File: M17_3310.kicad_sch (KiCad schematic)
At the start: 0 parts

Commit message: imported SA868 - thanks, edgetriggered
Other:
- sheet Interfaces ports: added 5V_USB, BOOT0, CLK, CMD, DAT0, DAT1, DAT2, DAT3, KEY_COLS, KEY_ROWS, PWM_BLIGHT, SD_DET, UDB_DM, USB_DP; removed none
- sheet MCU ports: added BOOT0, RF_RX, RF_TX, RTC_BATT, UDB_DM, USB_DP; removed none
- sheet PMU ports: added 5V_USB, PWR_ON, RTC_BATT, U_BATT, ~{CHG}; removed none
- sheet RF ports: added DEMOD_OUT, ENA, MOD_IN, PTT, PWR_SEL, RX, TX, U_BATT; removed none

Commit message: interfaces update
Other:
- sheet Interfaces ports: added DISP_D/C, DISP_SCK, DISP_SDIN, ~{DISP_CE}, ~{DISP_RST}; removed none
- sheet MCU ports: added DISP_DATA, DISP_D/C, DISP_SCK, KEY_COLS, KEY_ROWS, PTT_OUT, PWM_BLIGHT, RF_ENA, RF_PWR, ~{DISP_CE}, ~{DISP_RST}; removed none

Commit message: connections
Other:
- sheet MCU ports: added BSB_IN, BSB_OUT, PWR_ON, SD_CLK, SD_CMD, SD_D0, SD_D1, SD_D2, SD_D3, SD_DET, ~{CHG}; removed none

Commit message: audio part
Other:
- added sheet Audio (audio.kicad_sch)
- added sheet FIlters (filters.kicad_sch)
- sheet Interfaces ports: added VIBR; removed none
- sheet MCU ports: added AF_AMP_EN, MIC_IN, SPK_OUT, VIBR, ~{RF_ENA}; removed RF_ENA
- sheet RF ports: added ~{ENA}; removed ENA

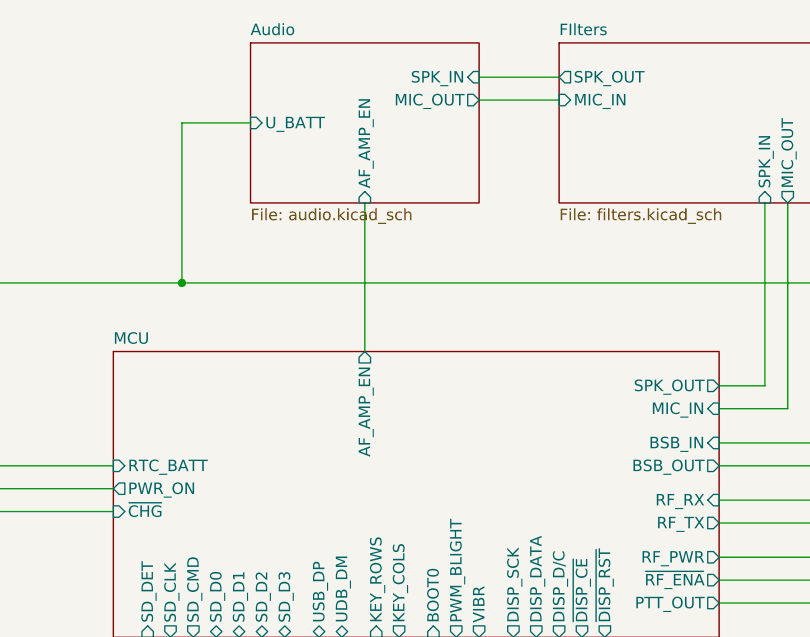
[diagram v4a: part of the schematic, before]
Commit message: spk/mic update
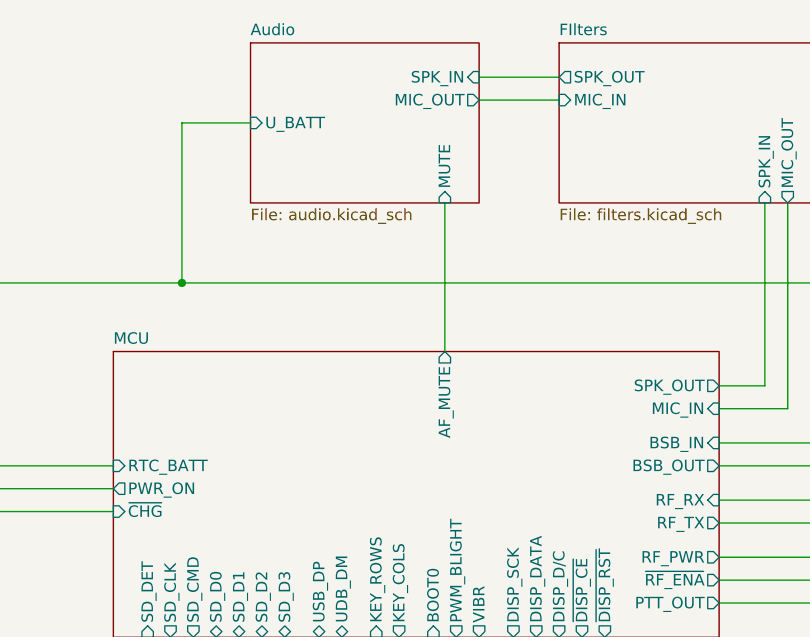
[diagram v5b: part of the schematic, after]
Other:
- sheet Audio ports: added MUTE; removed AF_AMP_EN
- sheet MCU ports: added AF_MUTE; removed AF_AMP_EN
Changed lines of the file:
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@@
 	(title_block
 		(title "Mainboard replacement for Nokia 3310")
-		(date "25-10-2024")
+		(date "28-10-2024")
 		(rev "Rev A")
 		(company "M17 Project")
@@
 	(wire
 		(pts
-			(xy 125.73 69.85) (xy 125.73 86.36)
+			(xy 134.62 69.85) (xy 134.62 86.36)
 		)
 		(stroke
@@
 			)
 		)
-		(pin "AF_AMP_EN" input
-			(at 125.73 69.85 270)
+		(pin "MUTE" input
+			(at 134.62 69.85 270)
 			(effects
 				(font
@@
 			)
 		)
-		(pin "AF_AMP_EN" output
-			(at 125.73 86.36 90)
-			(effects
-				(font
+		(pin "AF_MUTE" output
+			(at 134.62 86.36 90)
+			(effects
+				(font

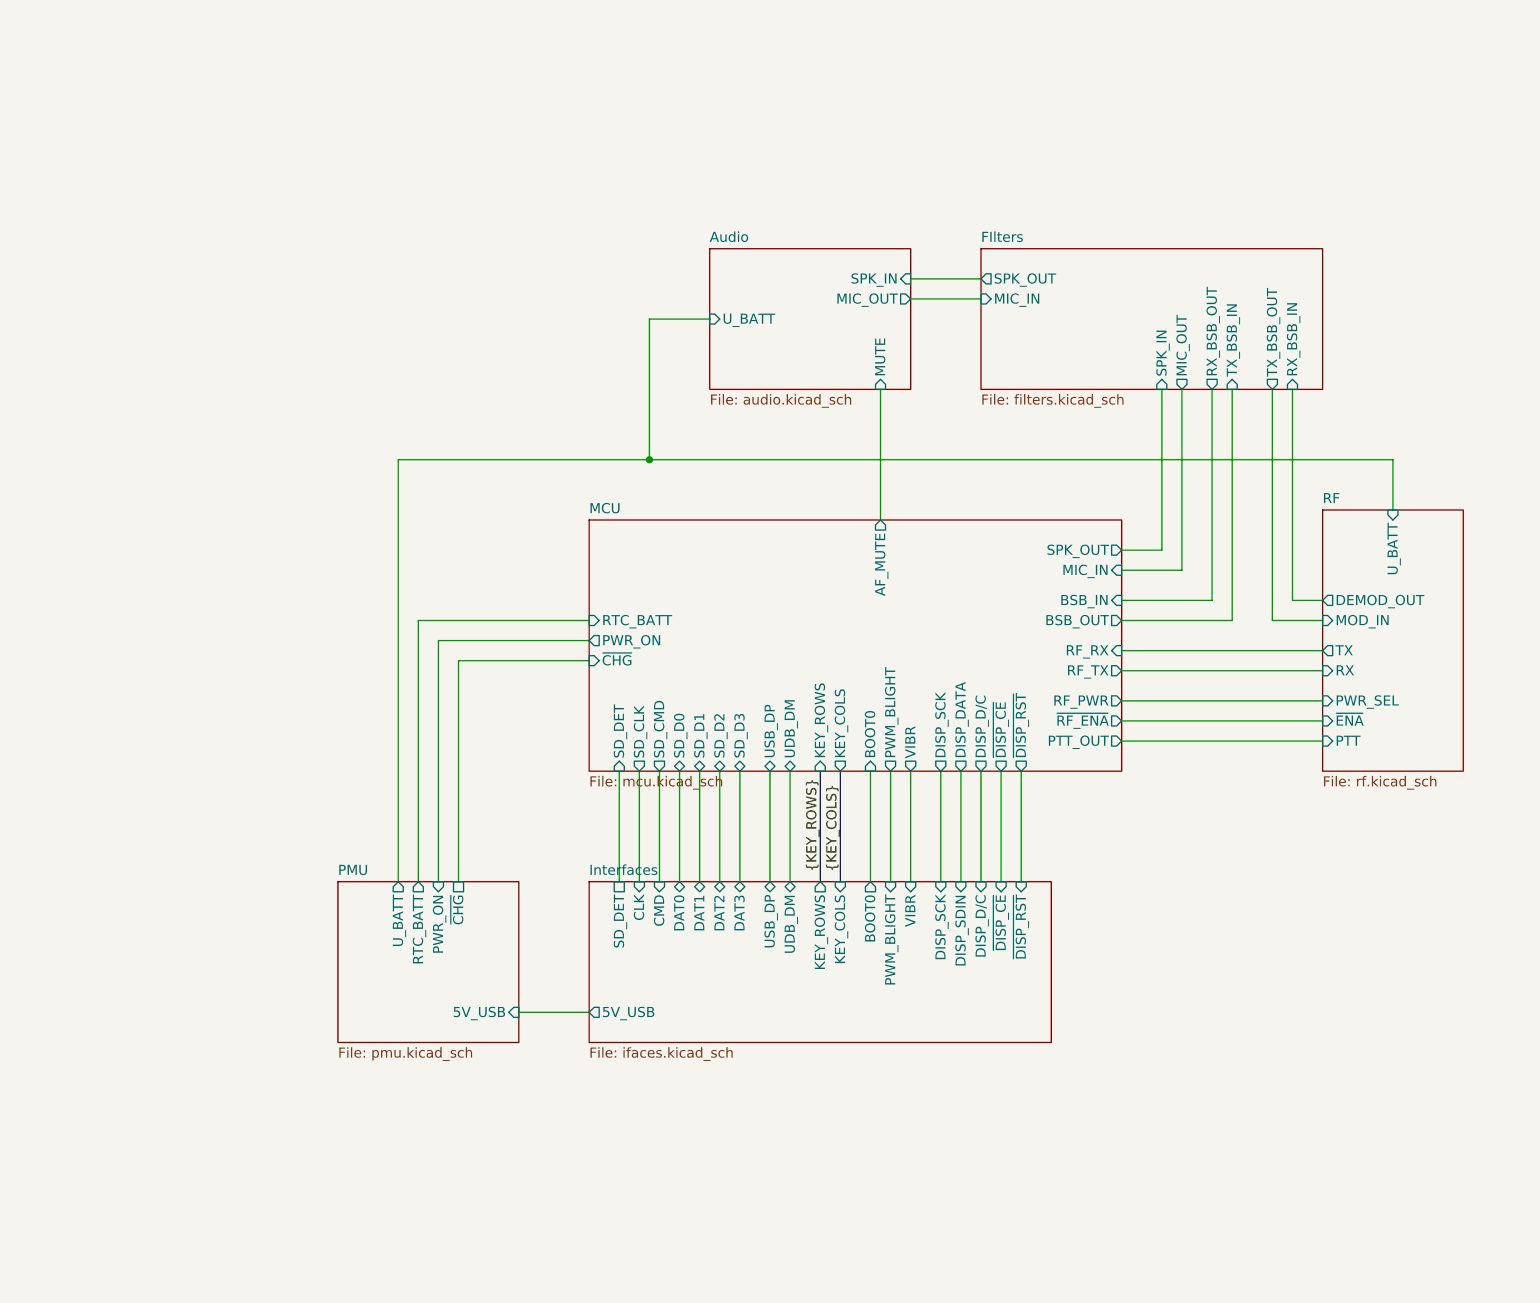
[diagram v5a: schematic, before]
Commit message: removed audio part
- added buzzer
- added battery voltage measurement
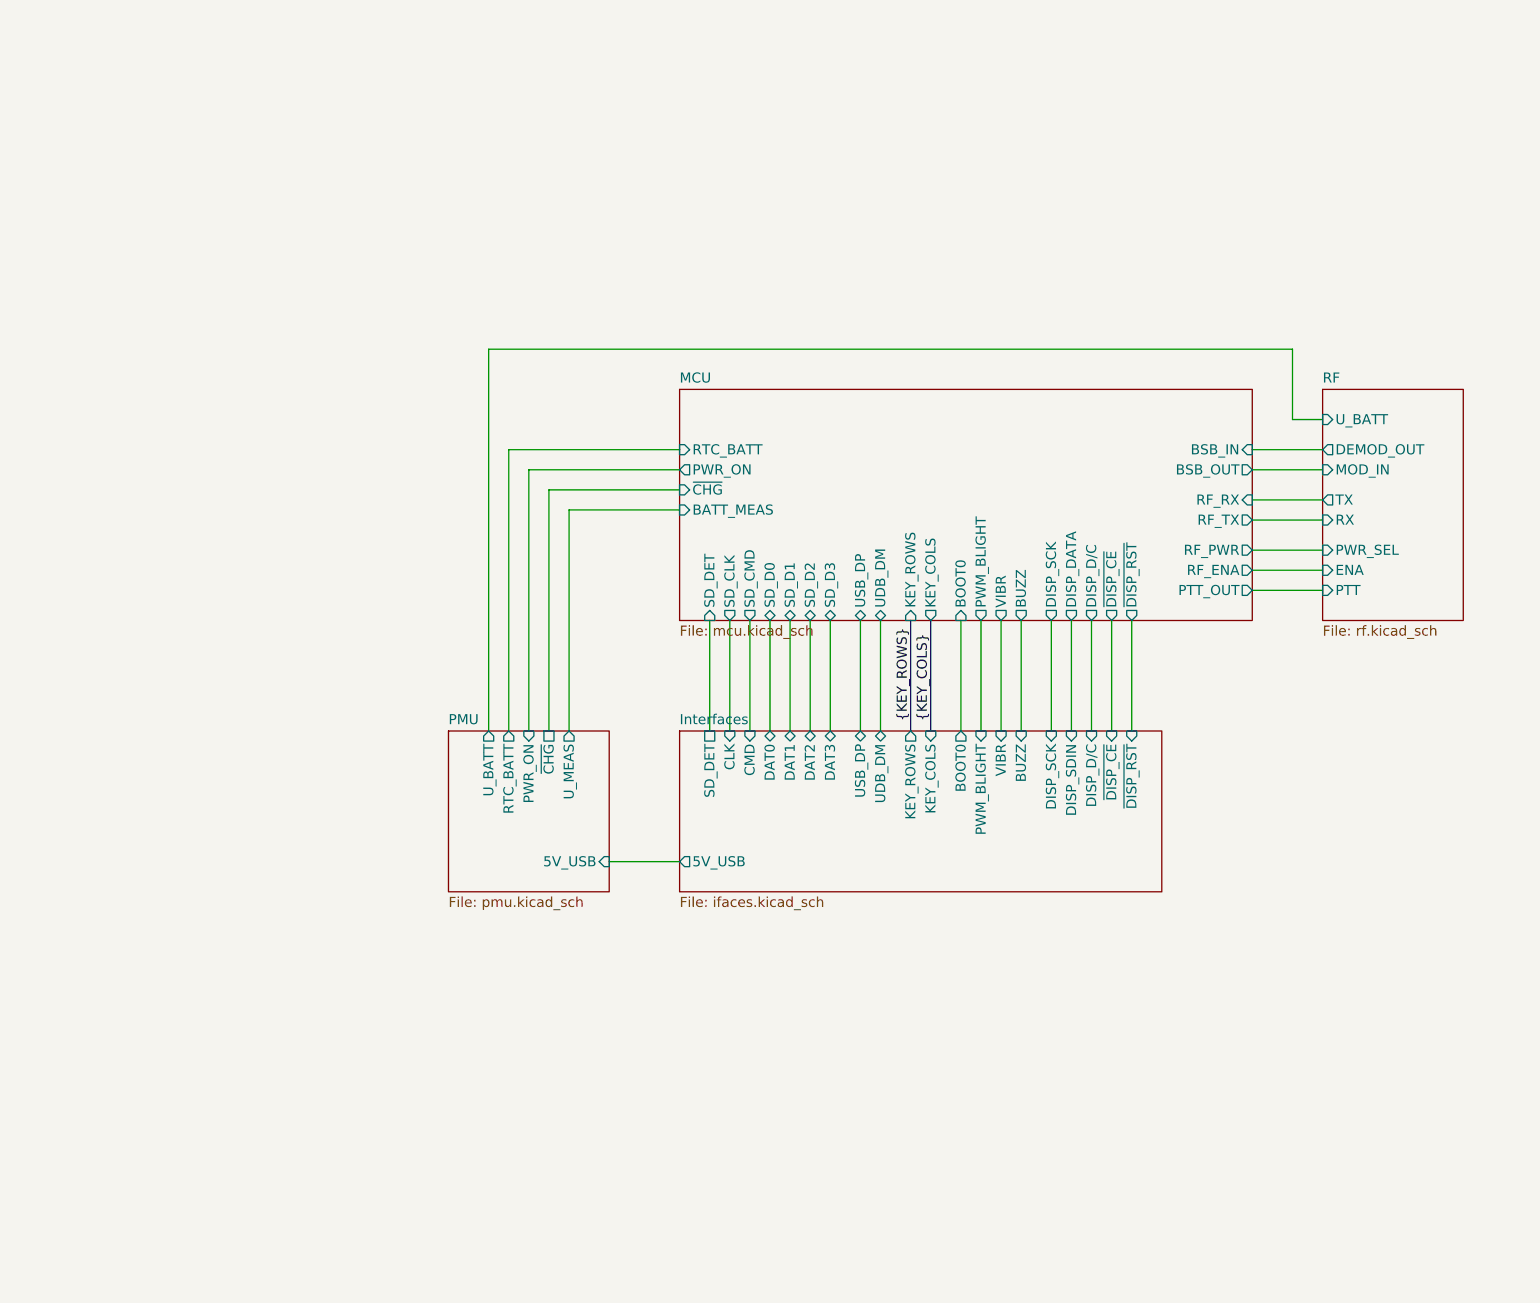
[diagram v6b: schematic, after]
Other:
- removed sheet Audio
- removed sheet FIlters
- sheet Interfaces ports: added BUZZ; removed none
- sheet MCU ports: added BATT_MEAS, BUZZ, RF_ENA; removed AF_MUTE, MIC_IN, SPK_OUT, ~{RF_ENA}
- sheet PMU ports: added U_MEAS; removed none
- sheet RF ports: added ENA; removed ~{ENA}

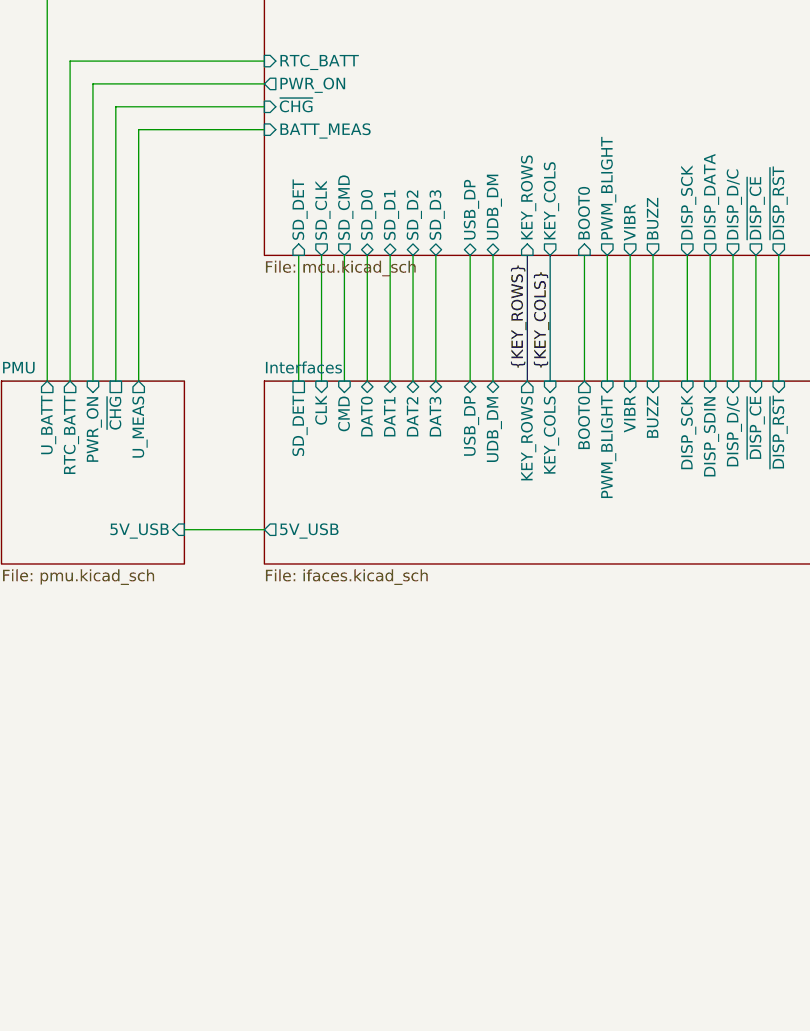
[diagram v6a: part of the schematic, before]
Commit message: mayhem
- removed sd card slot
- started pcb design
- added nice 3310 photos
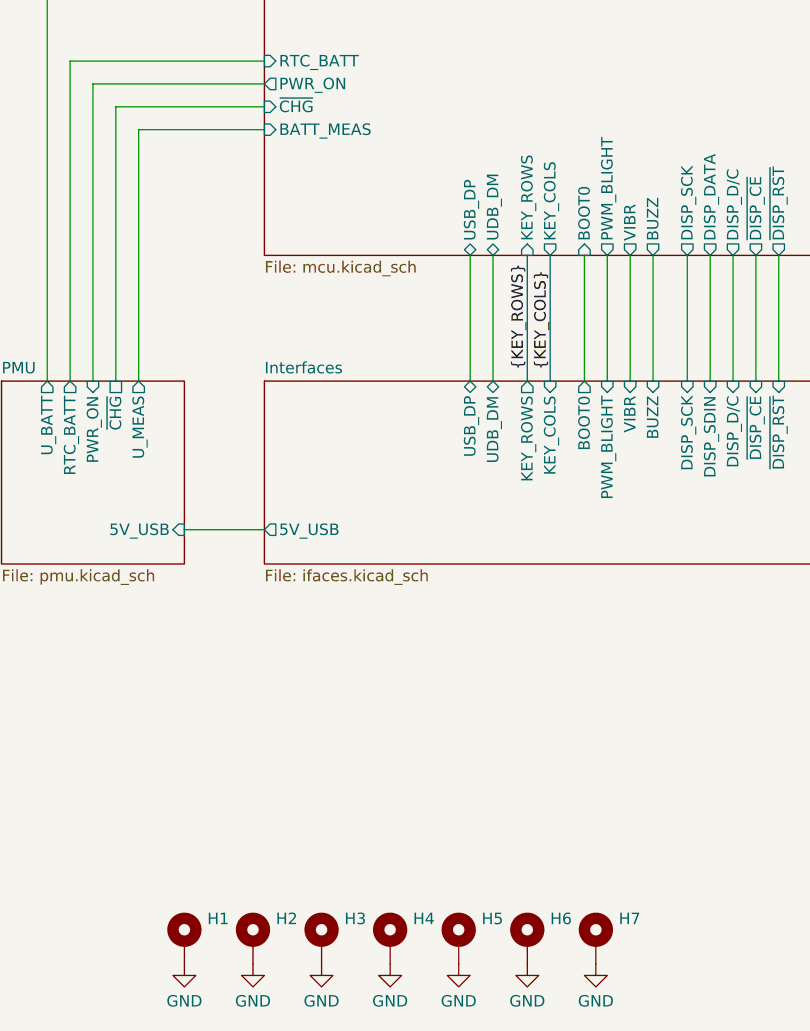
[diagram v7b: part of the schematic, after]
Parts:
- added H1, H2, H3, H4, H5, H6, H7: ~, Parts:2mm_mounting_hole_sig, symbol Mechanical:MountingHole_Pad
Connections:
- new net GND: H1.1, H2.1, H3.1, H4.1, H5.1, H6.1, H7.1
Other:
- sheet Interfaces ports: added none; removed CLK, CMD, DAT0, DAT1, DAT2, DAT3, SD_DET
- sheet MCU ports: added none; removed SD_CLK, SD_CMD, SD_D0, SD_D1, SD_D2, SD_D3, SD_DET
